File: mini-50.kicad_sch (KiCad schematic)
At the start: 1 part, among them U1 STM32H750VBT6

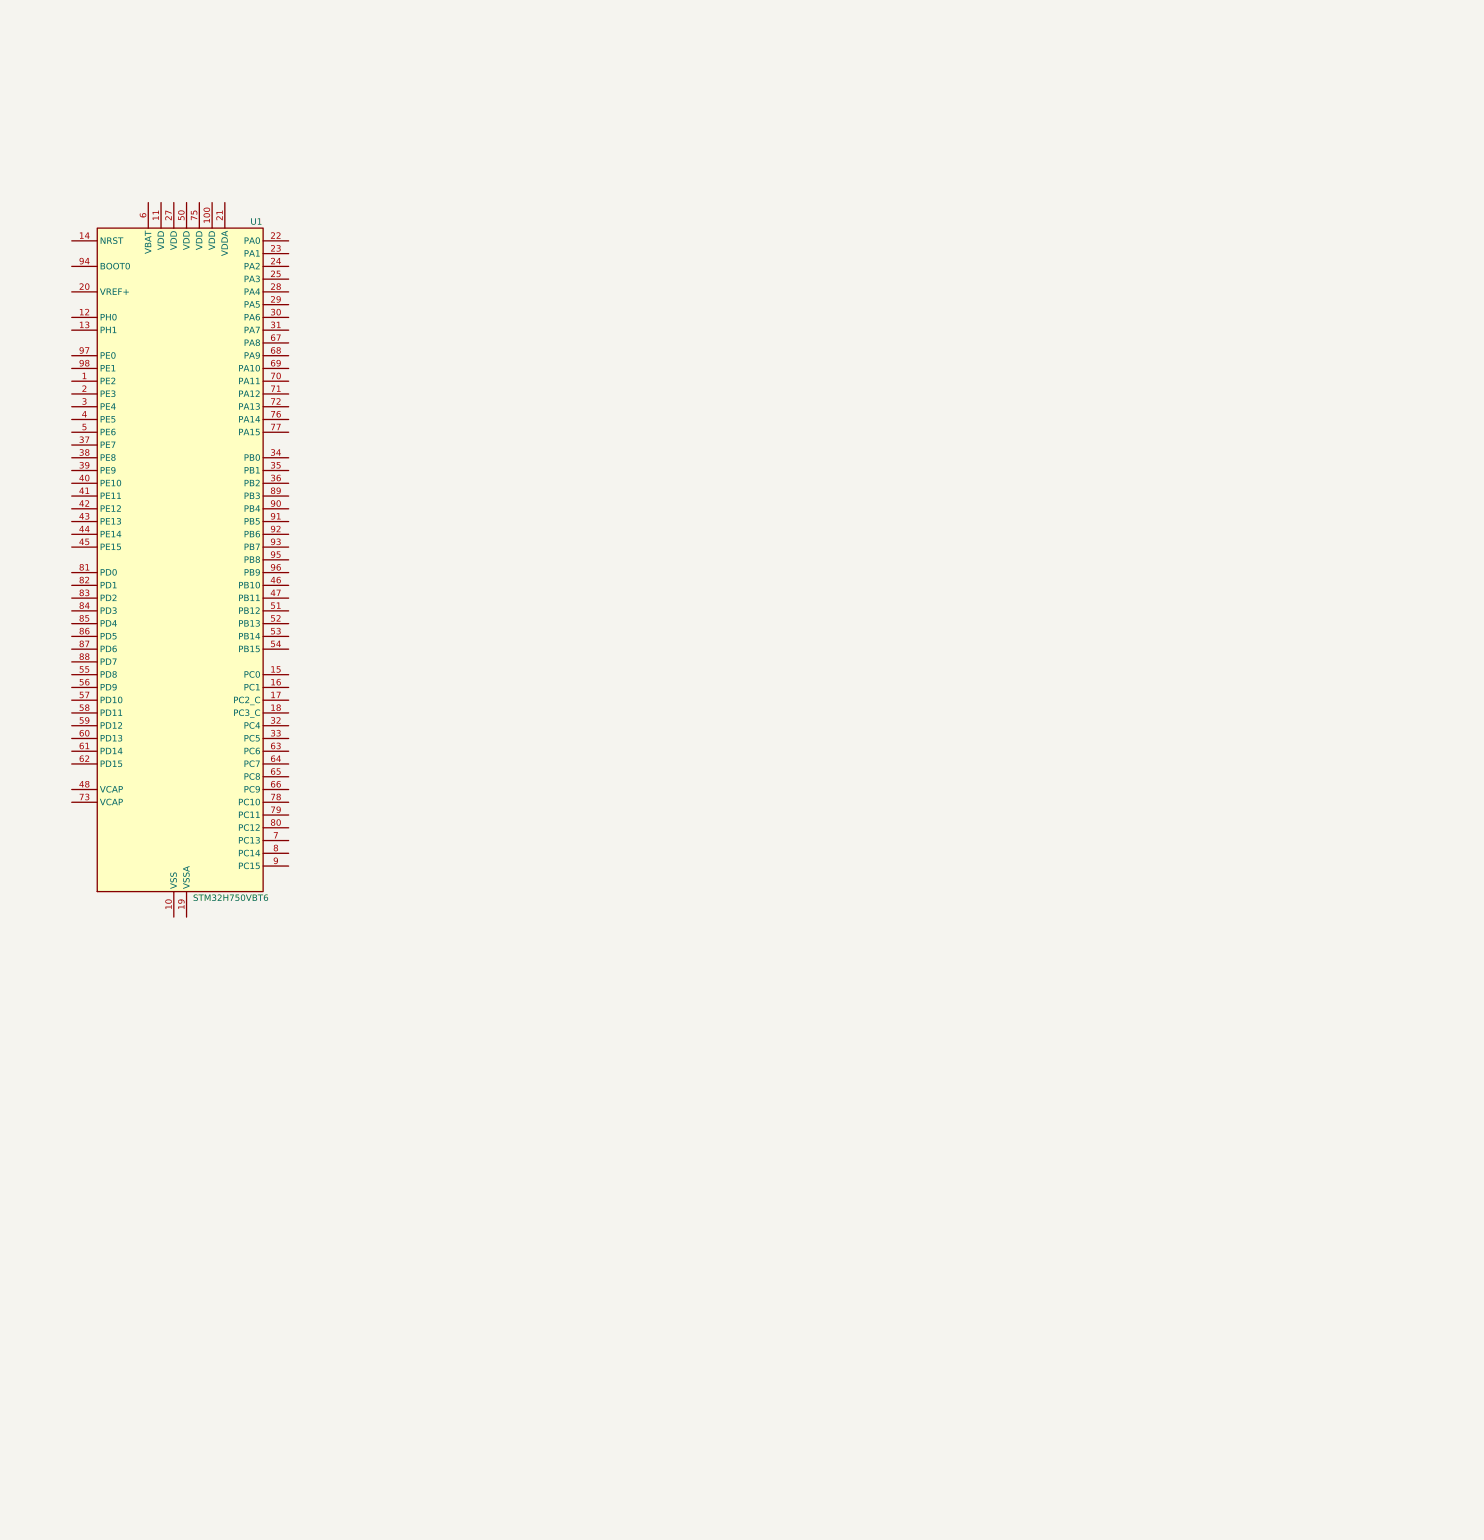
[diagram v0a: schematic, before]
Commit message: :sparkles: Add power management circuit for STM32
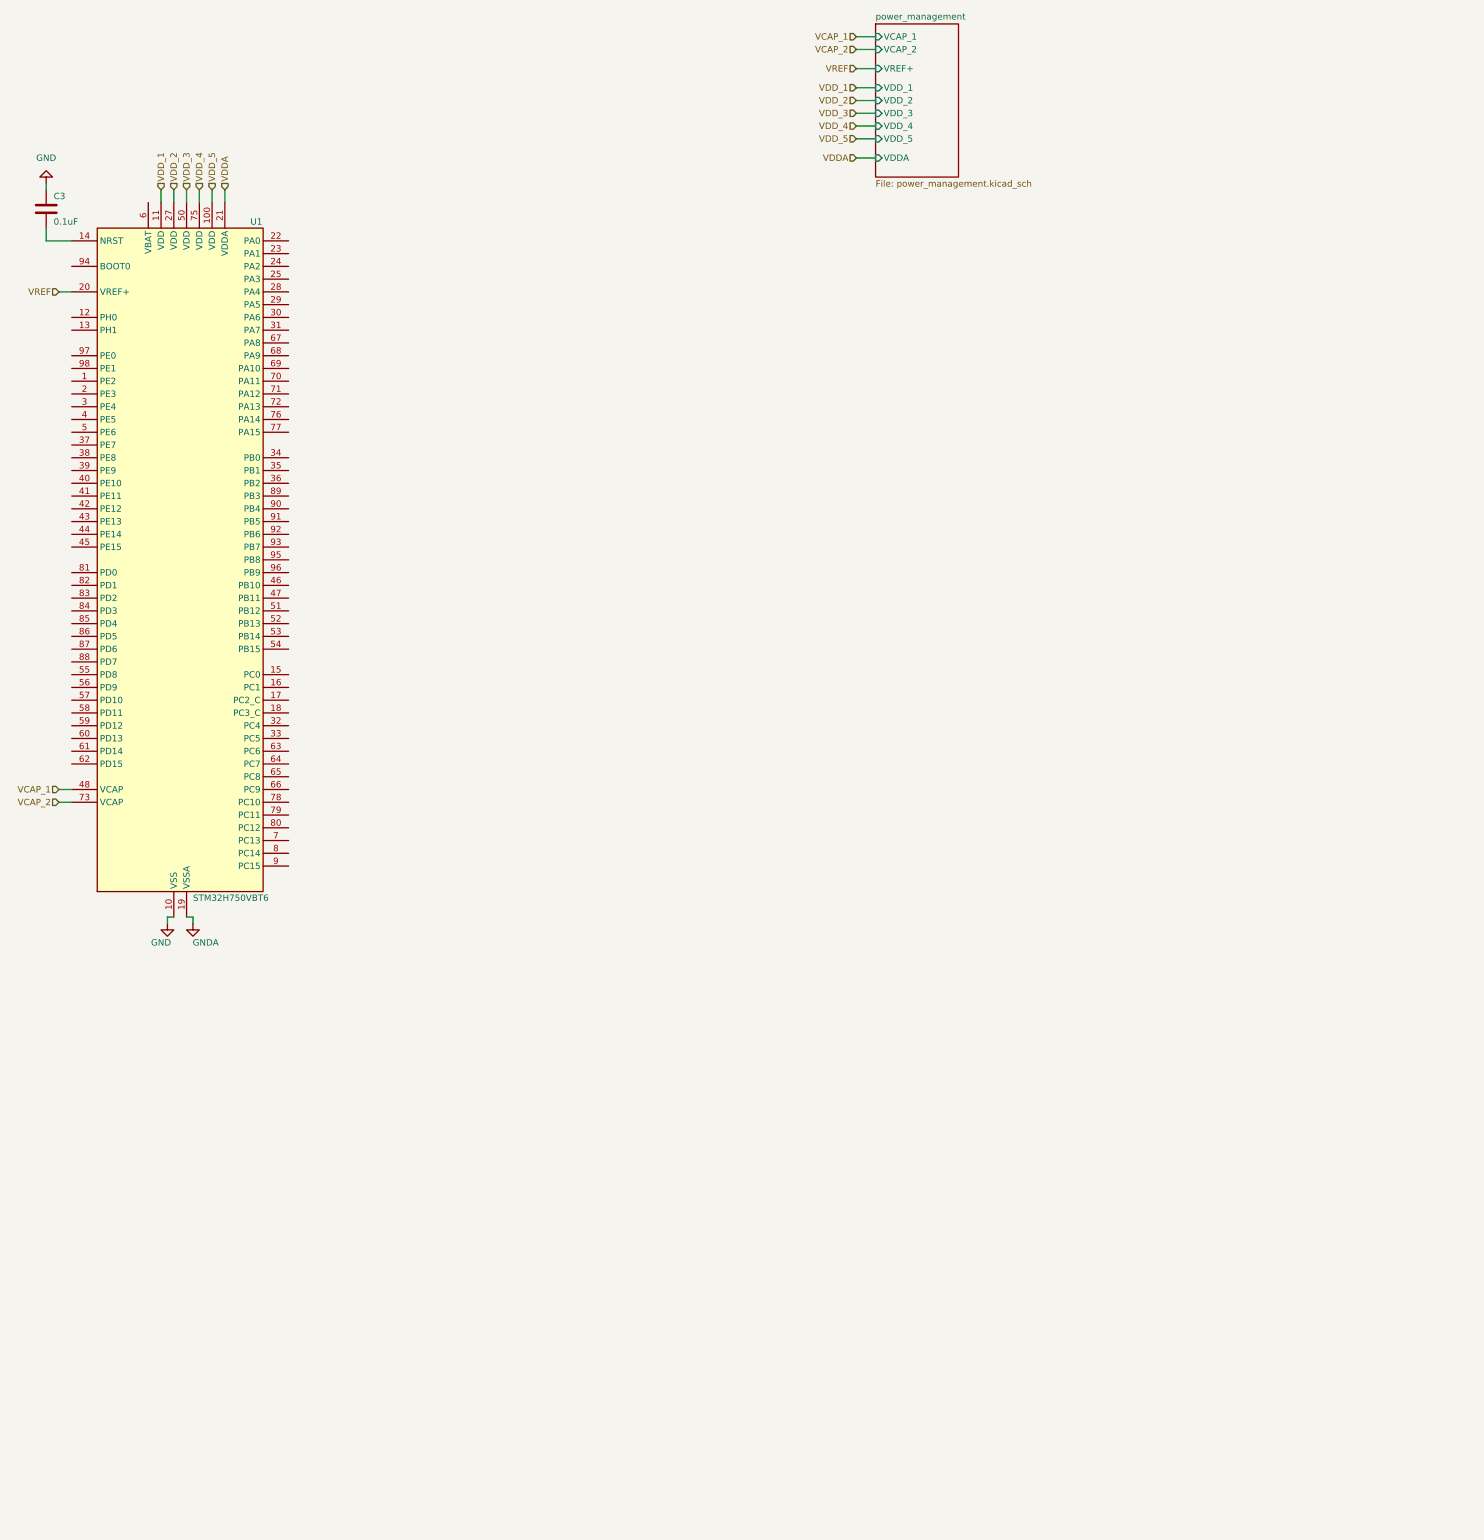
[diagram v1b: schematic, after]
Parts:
- added C3: 0.1uF, symbol Device:C
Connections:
- net GND: now reaches U1.10 (VSS), U1.26 (VSS), U1.49 (VSS), U1.74 (VSS), U1.99 (VSS)
- net GND: now also C3.2
- net VDD_5: now reaches U1.100 (VDD)
- net VDD_1: now reaches U1.11 (VDD)
- net at U1.14 (NRST): now also C3.1
- net GNDA: now reaches U1.19 (VSSA)
- net VREF: now reaches U1.20 (VREF+)
- net VDDA: now reaches U1.21 (VDDA)
- net VDD_2: now reaches U1.27 (VDD)
- net VCAP_1: now reaches U1.48 (VCAP)
- net VDD_3: now reaches U1.50 (VDD)
- net VCAP_2: now reaches U1.73 (VCAP)
- net VDD_4: now reaches U1.75 (VDD)
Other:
- added sheet power_management (power_management.kicad_sch)

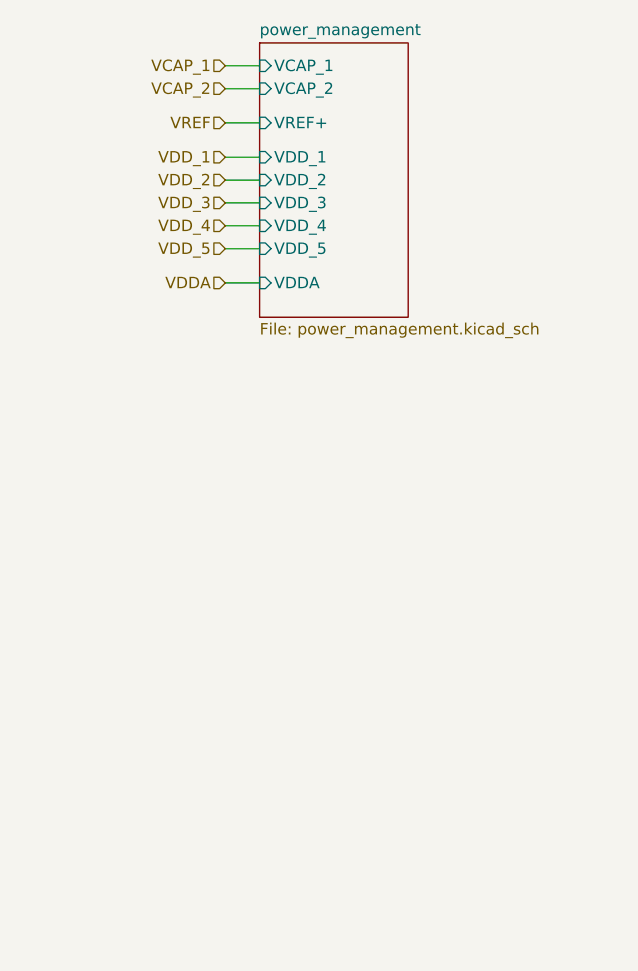
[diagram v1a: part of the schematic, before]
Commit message: ✨ Add initial bldc driver circuit
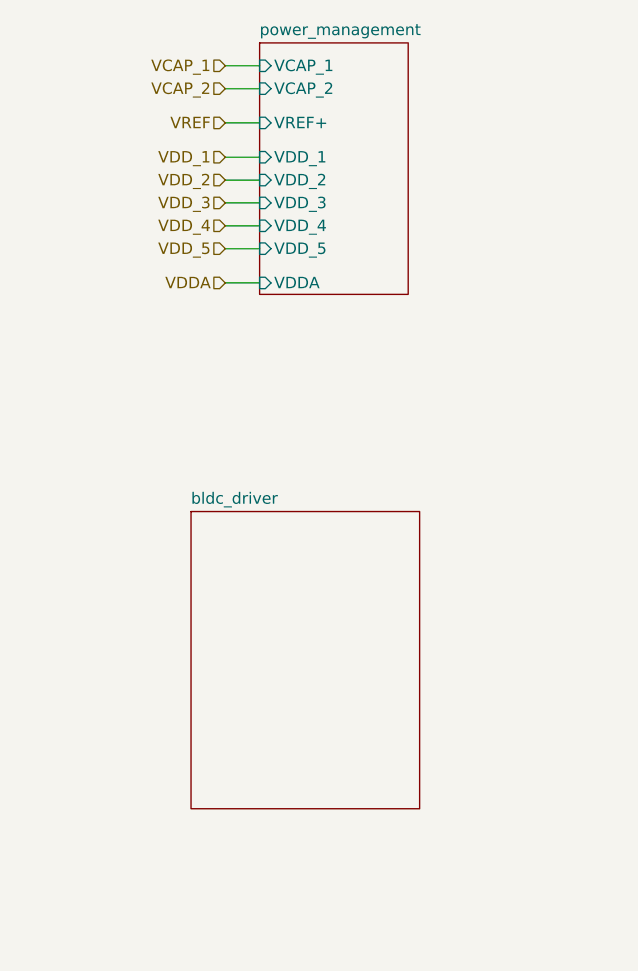
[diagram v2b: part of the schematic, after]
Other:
- added sheet bldc_driver (bldc_driver.kicad_sch)
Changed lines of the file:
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@@
     )
   )
-  (sheet (at 356.87 29.21) (size 16.51 30.48) (fields_autoplaced)
+  (sheet (at 349.25 81.28) (size 25.4 33.02) (fields_autoplaced)
+    (stroke (width 0.1524) (type solid))
+    (fill (color 0 0 0 0.0000))
+    (property "Sheetname" "bldc_driver" (at 349.25 80.5684 0)
+      (effects (font (size 1.27 1.27)) (justify left bottom))
+    )
+    (property "Sheetfile" "bldc_driver.kicad_sch" (at 349.25 114.8846 0)
+      (effects (font (size 1.27 1.27)) (justify left top) hide)
+    )
+    (instances
+      (project "mini-50"
+        (path "/a70b6d7d-99bd-40a0-9009-fac9fe2322d8" (page "3"))
+      )
+    )
+  )
+  (sheet (at 356.87 29.21) (size 16.51 27.94) (fields_autoplaced)
     (stroke (width 0.1524) (type solid))
     (fill (color 0 0 0 0.0000))
@@
       (effects (font (size 1.27 1.27)) (justify left bottom))
     )
-    (property "Sheetfile" "power_management.kicad_sch" (at 356.87 60.2746 0)
-      (effects (font (size 1.27 1.27)) (justify left top))
+    (property "Sheetfile" "power_management.kicad_sch" (at 356.87 57.7346 0)
+      (effects (font (size 1.27 1.27)) (justify left top) hide)
     )
     (pin "VREF+" input (at 356.87 38.1 180)

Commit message: 📂 Commit before drastic power board changes
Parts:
- removed C3: 0.1uF, symbol Device:C
- removed U1: STM32H750VBT6, Package_QFP:LQFP-100_14x14mm_P0.5mm, symbol MCU_ST_STM32H7:STM32H750VBTx
- added C1: 100nF, PCM_Capacitor_SMD_AKL:C_0201_0603Metric, symbol Device:C
- added U1: STM32H753IIKx, Package_BGA:UFBGA-201_10x10mm_Layout15x15_P0.65mm, symbol MCU_ST_STM32H7:STM32H753IIKx
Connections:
- net GND: now also C1.2, U1.D5 (VSS), U1.D6 (BOOT0), U1.D7 (VSS), U1.D8 (VSS), U1.D9 (VSS), U1.F10 (VSS), U1.F12 (VSS), U1.F2 (VSS), U1.F6 (VSS), U1.F7 (VSS), U1.F8 (VSS), U1.F9 (VSS), U1.G10 (VSS), U1.G12 (VSS), U1.G2 (VSS), U1.G6 (VSS), U1.G7 (VSS), U1.G8 (VSS), U1.G9 (VSS), U1.H10 (VSS), U1.H12 (VSS), U1.H6 (VSS), U1.H7 (VSS), U1.H8 (VSS), U1.H9 (VSS), U1.J10 (VSS), U1.J6 (VSS), U1.J7 (VSS), U1.J8 (VSS), U1.J9 (VSS), U1.K10 (VSS), U1.K6 (VSS), U1.K7 (VSS), U1.K8 (VSS), U1.K9 (VSS), U1.L4 (VSS), U1.M8 (VSS), U1.M9 (VSS)
- net GNDA: now also U1.M1 (VSSA), U1.N1 (VREF-)
- net VDDA: now also U1.R1 (VDDA)
- net VREF: now also U1.P1 (VREF+)
- new net: C1.1, U1.J1 (NRST)
- new net VCAP: U1.F13 (VCAP), U1.M10 (VCAP)
- new net VDD: U1.C1 (VBAT), U1.C5 (VDD), U1.C6 (PDR_ON), U1.C7 (VDD), U1.C8 (VDD), U1.C9 (VDD), U1.F3 (VDD), U1.G13 (VDD), U1.G3 (VDD), U1.J12 (VDD), U1.J13 (VDD), U1.K4 (VDD), U1.N10 (VDD), U1.N8 (VDD), U1.N9 (VDD)
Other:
- sheet bldc_driver ports: added CSENSE_A, CSENSE_B, CSENSE_C, HIN_A, HIN_B, HIN_C, LIN_A, LIN_B, LIN_C, PHASE_A, PHASE_B, PHASE_C; removed none
- sheet power_management ports: added VCAP, VDD; removed VCAP_1, VCAP_2, VDD_1, VDD_2, VDD_3, VDD_4, VDD_5
